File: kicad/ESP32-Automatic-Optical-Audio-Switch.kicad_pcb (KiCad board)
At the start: 2 copper layers, 45 x 38 mm, 30 parts, among them IC1 74LVC1G157GW,125, J1 FC684208R, J2 FC684208R, U1 74AHC1G4212, U2 74AHC1G4212, U3 ESP32-S3-ZERO, U4 FCR684208T, U5 AP2127K-3.3

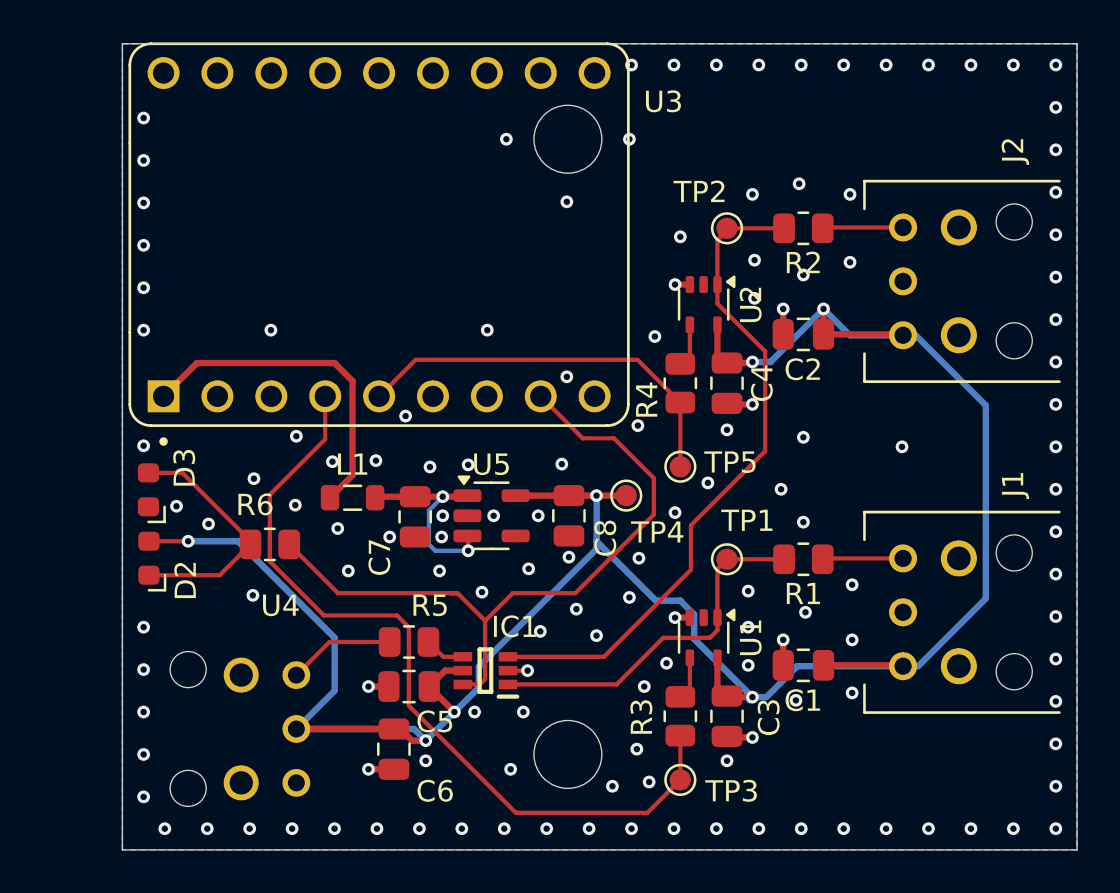
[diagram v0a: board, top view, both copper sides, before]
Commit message: Add system diagram and update PCB for ESP32 switch
Added a Draw.io system diagram for the ESP32 Optical Audio Switch. Updated the KiCad PCB and schematic files to reference the correct sheet file and replaced a capacitor footprint with the ESP32-C3-ZERO module footprint. Also updated .gitignore to exclude temporary Draw.io files.
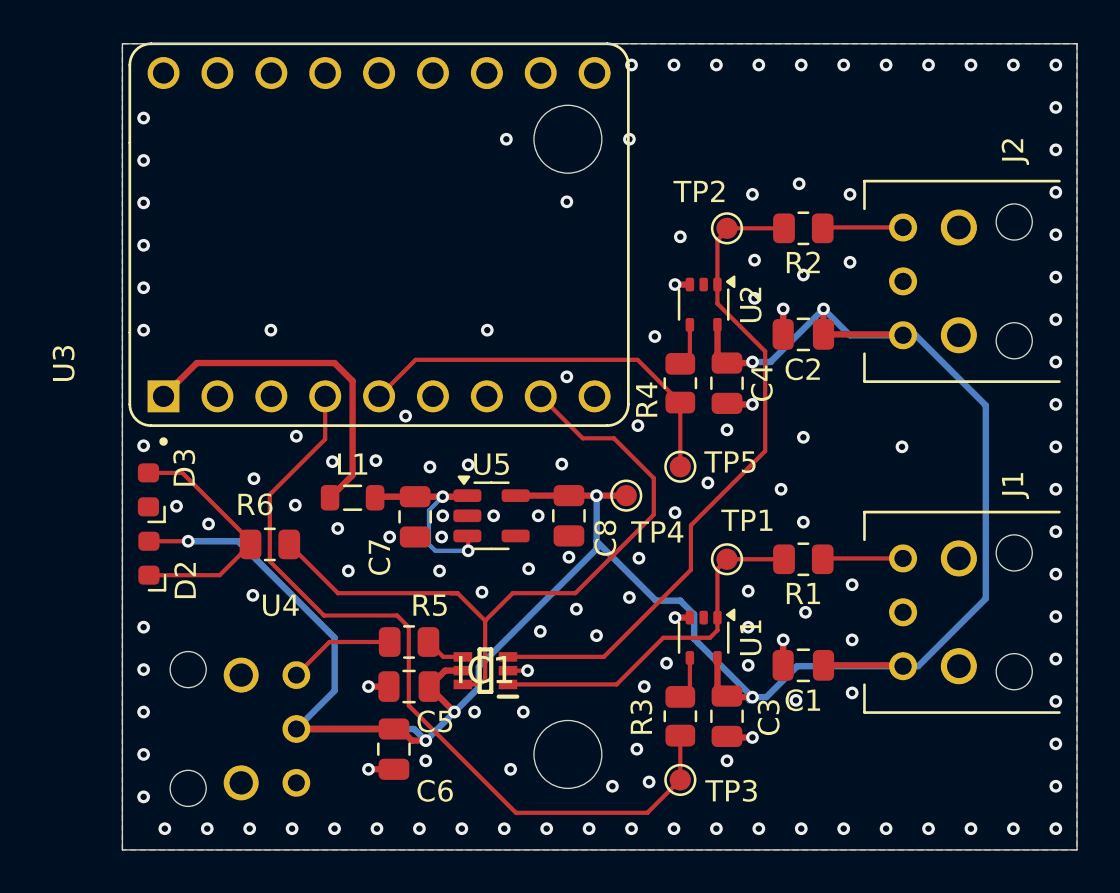
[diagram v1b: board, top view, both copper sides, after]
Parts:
- U3: value ESP32-S3-ZERO -> ESP32-C3-ZERO; footprint footprints:MODULE_ESP32-S3-ZERO -> footprints:MODULE_ESP32-C3-ZERO
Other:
- board text added: "Rev. 1 2025 uELKO"
- board text removed: "Rev. 01 2025 uELKO"
